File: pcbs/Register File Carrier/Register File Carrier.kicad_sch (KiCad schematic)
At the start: 6 parts, among them J1001 Conn_02x20_Odd_Even, J1002 Conn_02x20_Odd_Even, U1001 74HC245, U1002 74HC245, U1003 74HC245, U1004 74HC245

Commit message: Adding some more bits
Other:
- sheet Enabler ports: added Cycle[2..4], I[0..3], RegCLK, ~{AB_{Enable}}, ~{Enable}; removed none
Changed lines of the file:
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@@
 	(wire
 		(pts
+			(xy 121.92 140.97) (xy 137.16 140.97)
+		)
+		(stroke
+			(width 0)
+			(type default)
+		)
+	)
+	(wire
+		(pts
 			(xy 26.67 33.02) (xy 29.21 33.02)
 		)
@@
 		)
 	)
+	(wire
+		(pts
+			(xy 121.92 138.43) (xy 137.16 138.43)
+		)
+		(stroke
+			(width 0)
+			(type default)
+		)
+	)
 	(bus
 		(pts
@@
 	(label "Bo13"
 		(at 254 223.52 0)
+		(fields_autoplaced yes)
 		(effects
 			(font
@@
 	(label "Bo15"
 		(at 254 228.6 0)
+		(fields_autoplaced yes)
 		(effects
 			(font
@@
 	(label "Bo0"
 		(at 254 154.94 0)
+		(fields_autoplaced yes)
 		(effects
 			(font
@@
 	(label "Ao13"
 		(at 254 96.52 0)
+		(fields_autoplaced yes)
 		(effects
 			(font
@@
 	(label "Bo7"
 		(at 254 172.72 0)
+		(fields_autoplaced yes)
 		(effects
 			(font
@@
 	(label "Bo9"
 		(at 254 213.36 0)
+		(fields_autoplaced yes)
 		(effects
 			(font
@@
 	(label "Bo10"
 		(at 254 215.9 0)
+		(fields_autoplaced yes)
 		(effects
 			(font
@@
 	(label "Bo4"
 		(at 254 165.1 0)
+		(fields_autoplaced yes)
 		(effects
 			(font
@@
 	(label "Ao6"
 		(at 254 43.18 0)
+		(fields_autoplaced yes)
 		(effects
 			(font
@@
 	(label "Ao10"
 		(at 254 88.9 0)
+		(fields_autoplaced yes)
 		(effects
 			(font
@@
 	(label "Ao7"
 		(at 254 45.72 0)
+		(fields_autoplaced yes)
 		(effects
 			(font
@@
 	(label "Ao8"
 		(at 254 83.82 0)
+		(fields_autoplaced yes)
 		(effects
 			(font
@@
 	(label "Ao0"
 		(at 254 27.94 0)
+		(fields_autoplaced yes)
 		(effects
 			(font
@@
 	(label "Ao12"
 		(at 254 93.98 0)
+		(fields_autoplaced yes)
 		(effects
 			(font
@@
 	(label "Ao14"
 		(at 254 99.06 0)
+		(fields_autoplaced yes)
 		(effects
 			(font
@@
 	(label "Ao1"
 		(at 254 30.48 0)
+		(fields_autoplaced yes)
 		(effects
 			(font
@@
 	(label "Bo14"
 		(at 254 226.06 0)
+		(fields_autoplaced yes)
 		(effects
 			(font
@@
 	(label "Ao3"
 		(at 254 35.56 0)
+		(fields_autoplaced yes)
 		(effects
 			(font
@@
 	(label "Bo8"
 		(at 254 210.82 0)
+		(fields_autoplaced yes)
 		(effects
 			(font
@@
 	(label "Ao2"
 		(at 254 33.02 0)
+		(fields_autoplaced yes)
 		(effects
 			(font
@@
 	(label "Bo1"
 		(at 254 157.48 0)
+		(fields_autoplaced yes)
 		(effects
 			(font
@@
 	(label "Bo6"
 		(at 254 170.18 0)
+		(fields_autoplaced yes)
 		(effects
 			(font
@@
 	(label "Bo12"
 		(at 254 220.98 0)
+		(fields_autoplaced yes)
 		(effects
 			(font
@@
 	(label "Bo2"
 		(at 254 160.02 0)
+		(fields_autoplaced yes)
 		(effects
 			(font
@@
 	(label "Bo5"
 		(at 254 167.64 0)
+		(fields_autoplaced yes)
 		(effects
 			(font
@@
 	(label "Bo3"
 		(at 254 162.56 0)
+		(fields_autoplaced yes)
 		(effects
 			(font
@@
 	(label "Ao15"
 		(at 254 101.6 0)
+		(fields_autoplaced yes)
 		(effects
 			(font
@@
 	(label "Bo11"
 		(at 254 218.44 0)
+		(fields_autoplaced yes)
 		(effects
 			(font
@@
 	(label "Ao5"
 		(at 254 40.64 0)
+		(fields_autoplaced yes)
 		(effects
 			(font
@@
 	(label "Ao11"
 		(at 254 91.44 0)
+		(fields_autoplaced yes)
 		(effects
 			(font
@@
 	(label "Ao4"
 		(at 254 38.1 0)
+		(fields_autoplaced yes)
 		(effects
 			(font
@@
 	(label "Ao9"
 		(at 254 86.36 0)
+		(fields_autoplaced yes)
 		(effects
 			(font
@@
 	)
 	(sheet
-		(at 83.82 54.61)
-		(size 35.56 29.21)
+		(at 99.06 129.54)
+		(size 22.86 24.13)
 		(fields_autoplaced yes)
 		(stroke
@@
 		)
 		(property "Sheetname" "Enabler"
-			(at 83.82 53.8984 0)
+			(at 99.06 128.8284 0)
 			(effects
 				(font
@@
 		)
 		(property "Sheetfile" "enabler.kicad_sch"
-			(at 83.82 84.4046 0)
+			(at 99.06 154.2546 0)
 			(effects
 				(font
@@
 			)
 		)
+		(pin "Cycle[2..4]" input
+			(at 99.06 133.35 180)
+			(effects
+				(font
+					(size 1.27 1.27)
+				)
+				(justify left)
+			)
+		)
+		(pin "~{Enable}" output
+			(at 121.92 151.13 0)
+			(effects
+				(font
+					(size 1.27 1.27)
+				)
+				(justify right)
+			)
+		)
+		(pin "I[0..3]" input
+			(at 99.06 139.7 180)
+			(effects
+				(font
+					(size 1.27 1.27)
+				)
+				(justify left)
+			)
+		)
+		(pin "~{AB_{Enable}}" output
+			(at 121.92 140.97 0)
+			(effects
+				(font
+					(size 1.27 1.27)
+				)
+				(justify right)
+			)
+		)
+		(pin "RegCLK" output
+			(at 121.92 138.43 0)
+			(effects
+				(font
+					(size 1.27 1.27)
+				)
+				(justify right)
+			)
+		)

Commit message: Starting to route
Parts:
- removed U1001, U1002, U1003, U1004: 74HC245, Package_SO:SOIC-20W_7.5x12.8mm_P1.27mm, symbol 74xx:74HC245
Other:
- added sheet Output Buffer A (outputbuffer.kicad_sch)
- added sheet Output Buffer B (outputbuffer.kicad_sch)

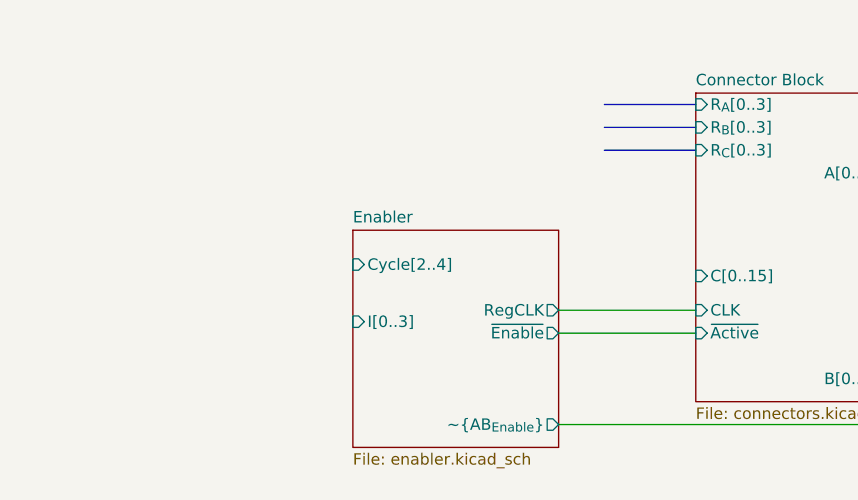
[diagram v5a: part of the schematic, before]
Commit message: Setting up some LEDs
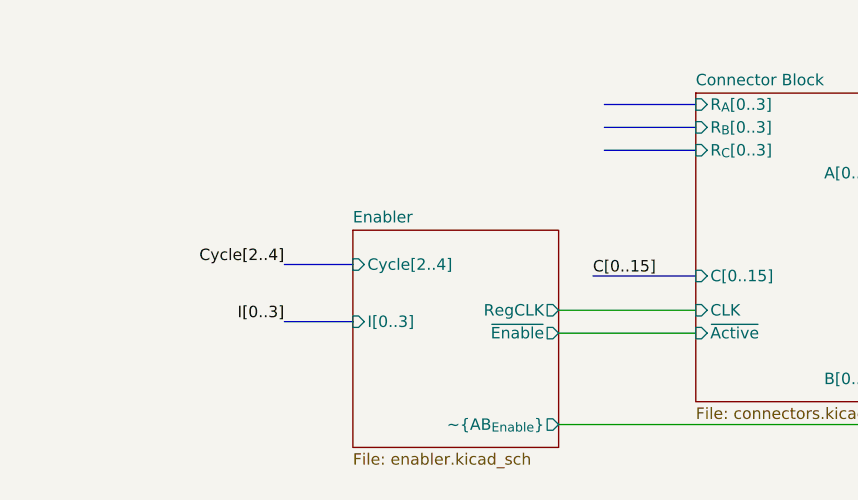
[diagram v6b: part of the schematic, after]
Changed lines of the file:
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@@
+		)
+	)
+	(bus
+		(pts
+			(xy 125.73 134.62) (xy 137.16 134.62)
+		)
+		(stroke
+			(width 0)
+			(type default)
 		)
 	)
@@
 		)
 	)
+	(bus
+		(pts
+			(xy 91.44 133.35) (xy 99.06 133.35)
+		)
+		(stroke
+			(width 0)
+			(type default)
+		)
+	)
 	(wire
 		(pts
@@
 		(pts
 			(xy 41.91 97.79) (xy 44.45 97.79)
+		)
+		(stroke
+			(width 0)
+			(type default)
+		)
+	)
+	(bus
+		(pts
+			(xy 91.44 139.7) (xy 99.06 139.7)
 		)
 		(stroke
@@
 		)
 	)
+	(label "I[0..3]"
+		(at 91.44 139.7 180)
+		(fields_autoplaced yes)
+		(effects
+			(font
+				(size 1.27 1.27)
+			)
+			(justify right bottom)
+		)
+	)
 	(label "Cycle0"
 		(at 26.67 138.43 180)
@@
 		)
 	)
+	(label "Cycle[2..4]"
+		(at 91.44 133.35 180)
+		(fields_autoplaced yes)
+		(effects
+			(font
+				(size 1.27 1.27)
+			)
+			(justify right bottom)
+		)
+	)
 	(label "Ao[0..15]"
 		(at 215.9 123.19 0)
@@
 		(fields_autoplaced yes)
 		(effects
+			(font
+				(size 1.27 1.27)
+			)
+			(justify left bottom)
+		)
+	)
+	(label "C[0..15]"
+		(at 125.73 134.62 0)
+		(fields_autoplaced yes)
+		(effects

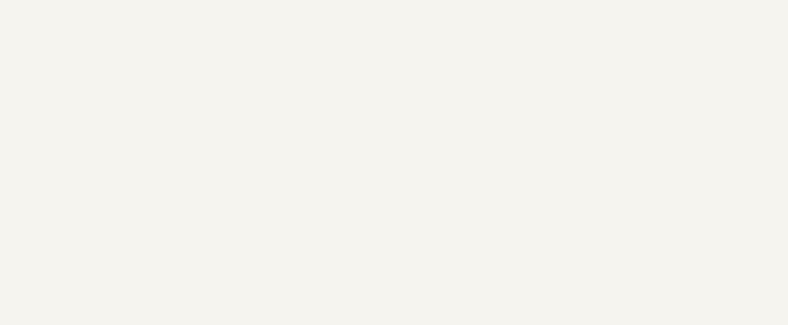
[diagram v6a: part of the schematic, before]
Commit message: Adding mounting holes; thinking about needs
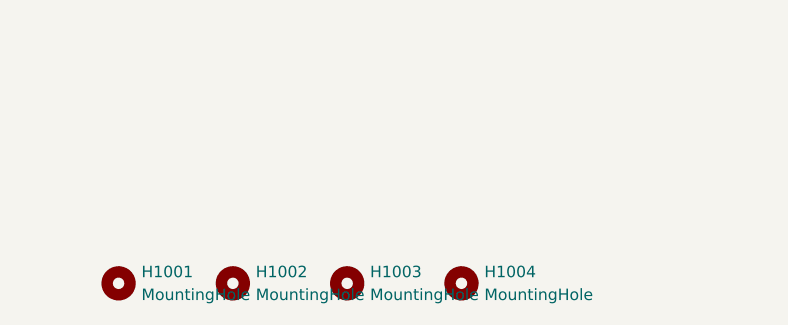
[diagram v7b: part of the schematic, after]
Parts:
- added H1001, H1002, H1003, H1004: MountingHole, MountingHole:MountingHole_2.7mm_M2.5_ISO7380, symbol Mechanical:MountingHole

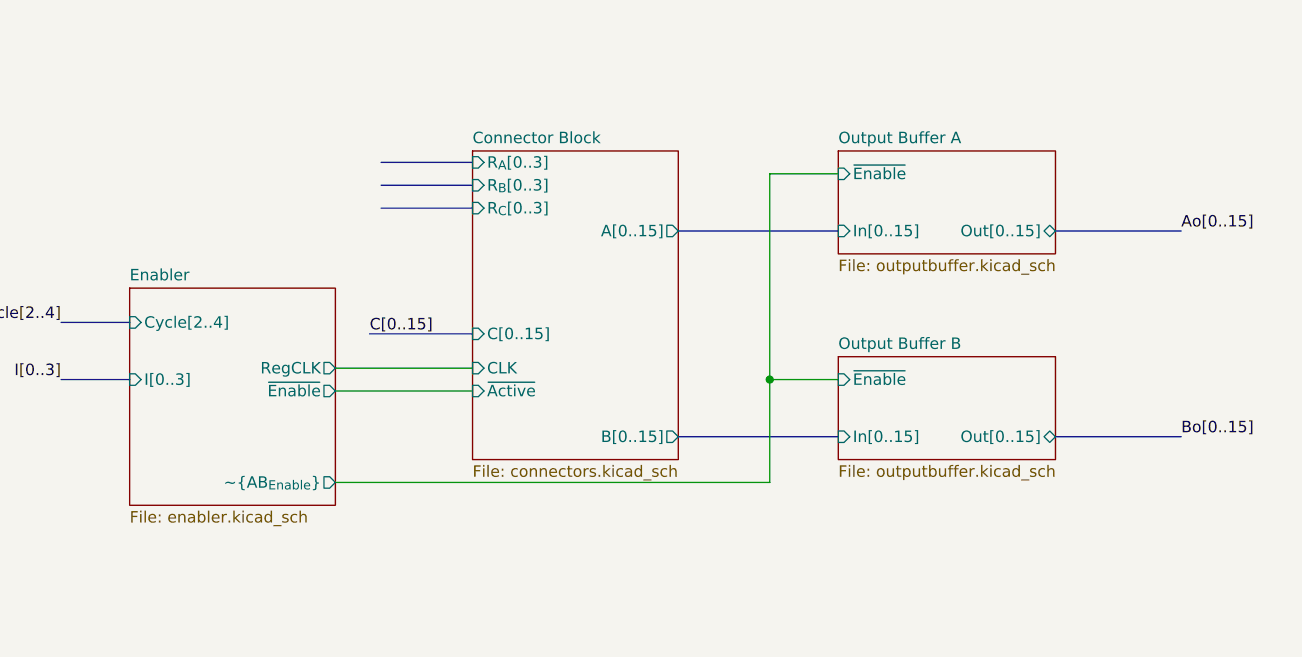
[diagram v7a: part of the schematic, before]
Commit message: Output buffers were a bad idea which were about to cause trouble
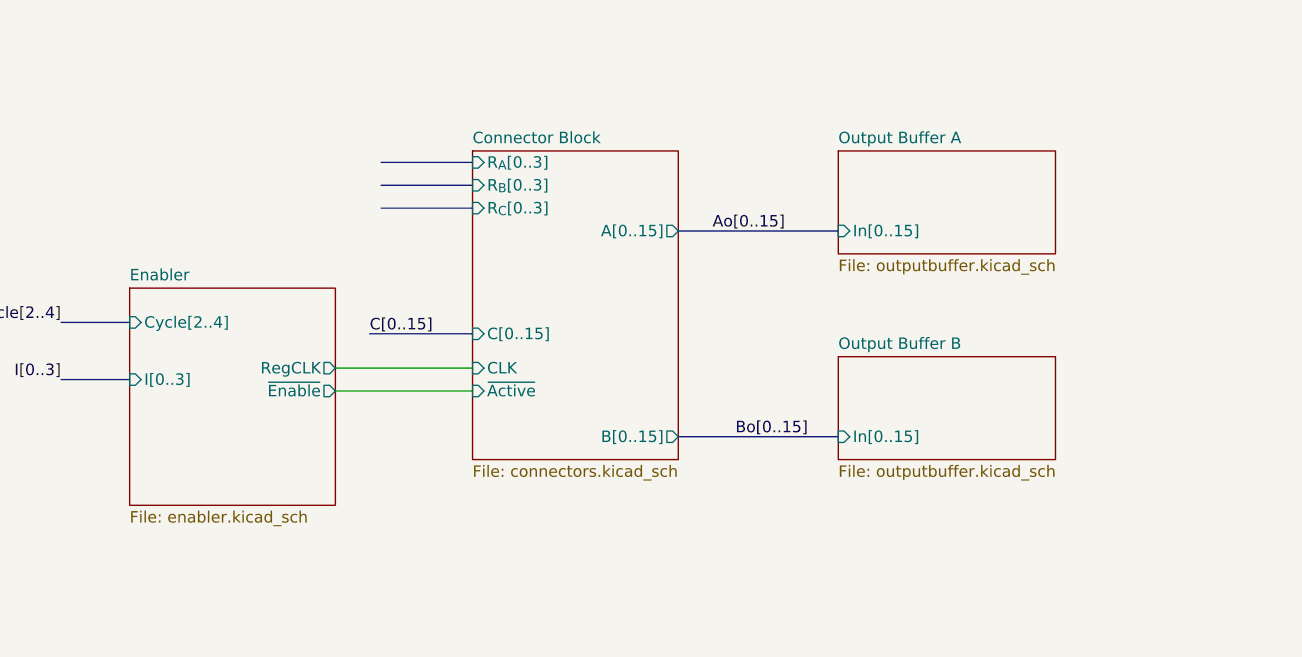
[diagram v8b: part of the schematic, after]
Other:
- sheet Enabler ports: added none; removed ~{AB_{Enable}}
- sheet Output Buffer A ports: added none; removed Out[0..15], ~{Enable}
- sheet Output Buffer B ports: added none; removed Out[0..15], ~{Enable}
